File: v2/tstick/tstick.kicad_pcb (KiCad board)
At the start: 2 copper layers, 25 x 129 mm, 26 parts, among them SW1 SW_PUSH, SW2 SW_PUSH, SW21 SW_SPDT, SW3 SW_PUSH, SW4 RotaryEncoder, U2 MCP1700x-180xxTT

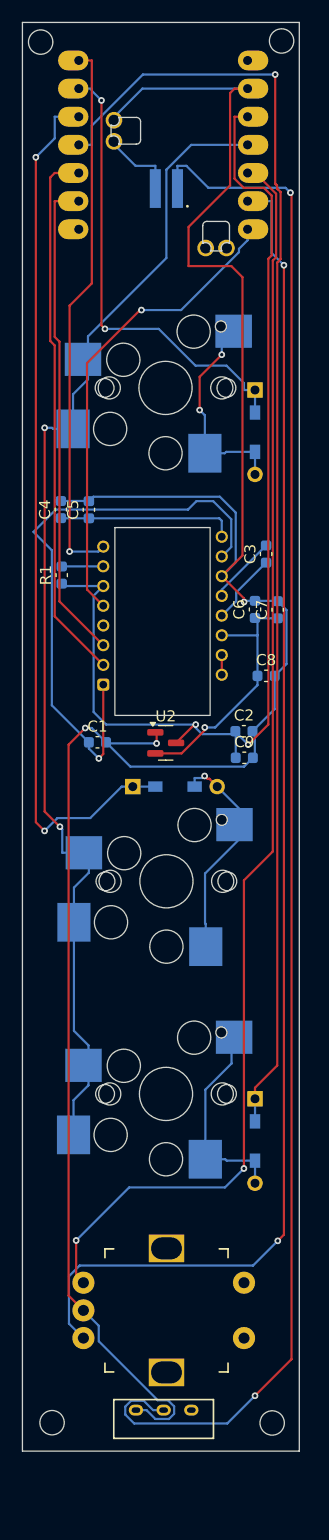
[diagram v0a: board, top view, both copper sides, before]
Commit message: 25mmボールが入るように修正
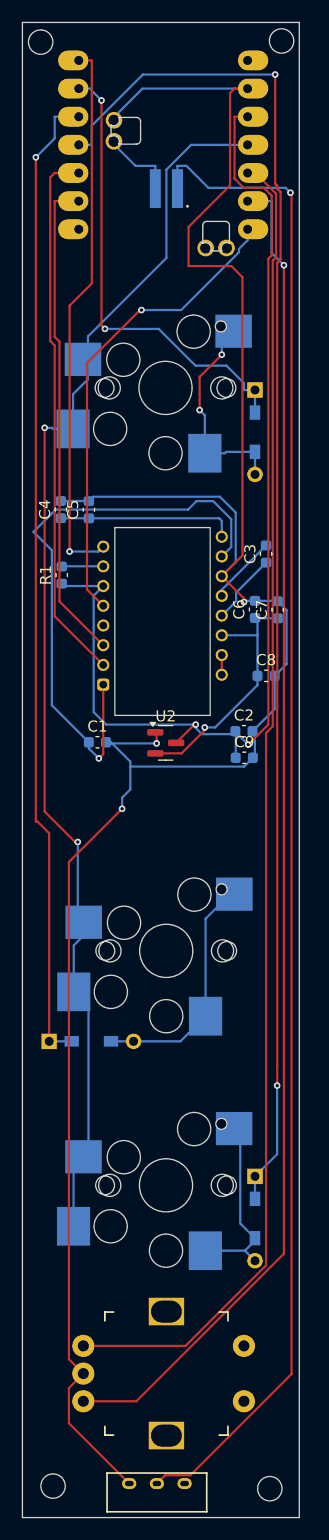
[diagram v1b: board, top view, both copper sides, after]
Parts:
- moved D2 24.2 mm to (93.2, 128.0)
- moved SW3 8.25 mm to (100.0, 141.0)
- moved D3 7.00 mm to (108.0, 144.0)
- moved SW21 6.66 mm to (99.1, 169.0)
- moved SW2 6.28 mm to (100.0, 119.8)
- moved Ref** 5.94 mm to (109.3, 168.4)
- moved Ref** 5.72 mm to (89.8, 168.2)
- moved SW4 5.71 mm to (100.0, 158.0)
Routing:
- net Row1: track 79.4 -> 89.1 mm, vias 2 -> 1
- net Row2: track 117.4 -> 124.4 mm, vias 1 -> 2
- net Col0: track 106.3 -> 113.3 mm
- net REA: track 114.5 -> 120.0 mm, vias 2 -> 0
- net Net-(BT1--): track 141.7 -> 136.8 mm, vias 2 -> 1
- net GND: track 204.0 -> 201.2 mm
- net REB: track 123.0 -> 121.3 mm, vias 2 -> 1
- net Net-(D3-A): track 18.6 -> 17.2 mm
- net Net-(D2-A): track 20.5 -> 21.4 mm, vias 1 -> 0
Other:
- board size 25 x 129 mm -> 25 x 135 mm

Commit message: fix
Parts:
- C1, C2, C3, C4, C5, C6, C7, C8, C9, R1, U2: moved to B.Cu
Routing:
- net +1v9: track 23.2 -> 24.3 mm, vias 1 -> 2
- net GND: track 201.2 -> 200.9 mm, vias 3 -> 2
